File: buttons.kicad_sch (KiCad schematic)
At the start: 11 parts, among them SW1 power, SW2 up, SW3 down, SW4 left, SW5 rigth

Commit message: Fix KiCad 10 footprint library: register kiC library, fix schematic references
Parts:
- SW1, SW3, SW4, SW5: footprint Button_Switch_SMD:SW_Push_1P1T_NO_6x6mm_H9.5mm -> kiC:SW_Push_1P1T_NO_6x6mm_H9.5mm
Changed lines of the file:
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@@
 			)
 		)
-		(property "Footprint" "Button_Switch_SMD:SW_Push_1P1T_NO_6x6mm_H9.5mm"
+		(property "Footprint" "kiC:SW_Push_1P1T_NO_6x6mm_H9.5mm"
 			(at 212.09 110.49 0)
 			(hide yes)
@@
 			)
 		)
-		(property "Footprint" "Button_Switch_SMD:SW_Push_1P1T_NO_6x6mm_H9.5mm"
+		(property "Footprint" "kiC:SW_Push_1P1T_NO_6x6mm_H9.5mm"
 			(at 137.16 77.47 0)
 			(hide yes)
@@
 			)
 		)
-		(property "Footprint" "Button_Switch_SMD:SW_Push_1P1T_NO_6x6mm_H9.5mm"
+		(property "Footprint" "kiC:SW_Push_1P1T_NO_6x6mm_H9.5mm"
 			(at 144.78 123.19 0)
 			(hide yes)
@@
 			)
 		)
-		(property "Footprint" "Button_Switch_SMD:SW_Push_1P1T_NO_6x6mm_H9.5mm"
+		(property "Footprint" "kiC:SW_Push_1P1T_NO_6x6mm_H9.5mm"
 			(at 212.09 97.79 0)
 			(hide yes)

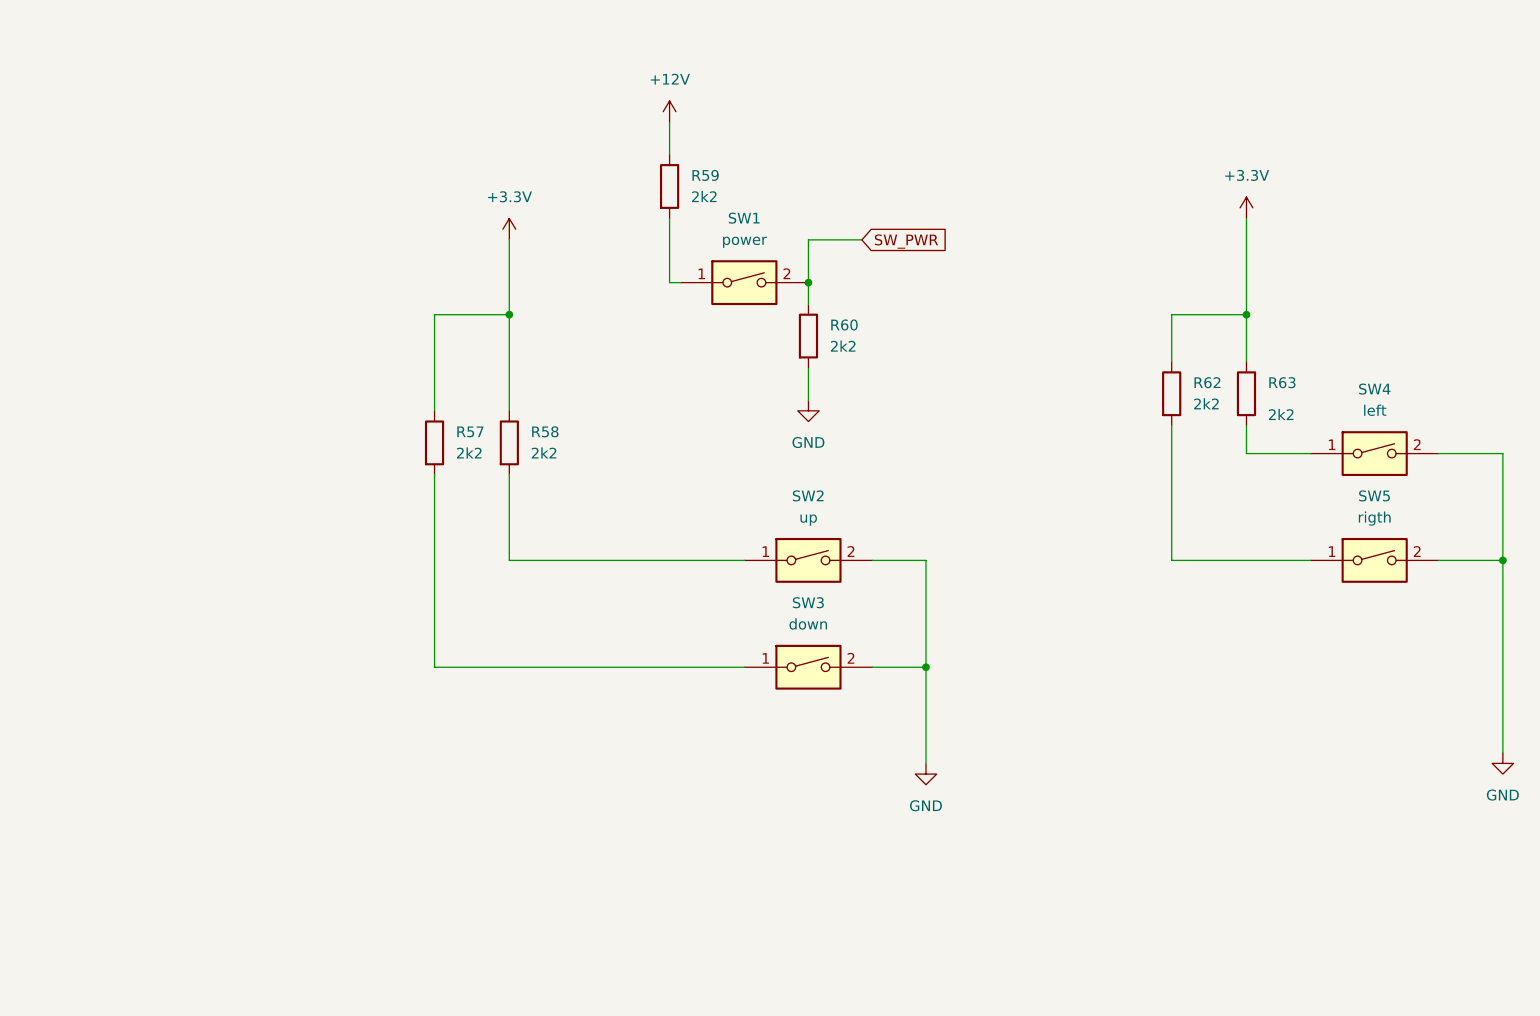
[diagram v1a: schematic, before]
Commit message: feat: 25 hierarchical labels for 5 Pololus + fix J4/J15/J17/TP17 footprints + USB pin6→SH
- pololu.kicad_sch: 5→25 hierarchical labels (reset_N, sleep_N, enable_N, step_N, dir_N) with wires to each Pololu A4988
- pololu.kicad_sch: J17 footprint kiC:PinHeader → Library:PinHeader_1x06_P2.54mm_Vertical
- cnc_pic32.kicad_sch: expanded Pololu sheet box with 25 named sheet pins
- buttons.kicad_sch: all SW switches → Button_Switch_SMD:SW_SPST_CK_RS282G05A3
- tp_ft232.kicad_sch: kiC:pad_0508 + kiC:Pin_D1.5mmx1mm → Library:connector_pin1
- usb_conector_Ft232.kicad_sch: J4/J15 kiC:Pin_D1.5mmx1mm → Library:connector_pin1, J5 pin 6→SH
- Usb_pic32.kicad_sch: TP17 kiC:Pin_D1.5mmx1mm → Library:connector_pin1, J18 pin 6→SH
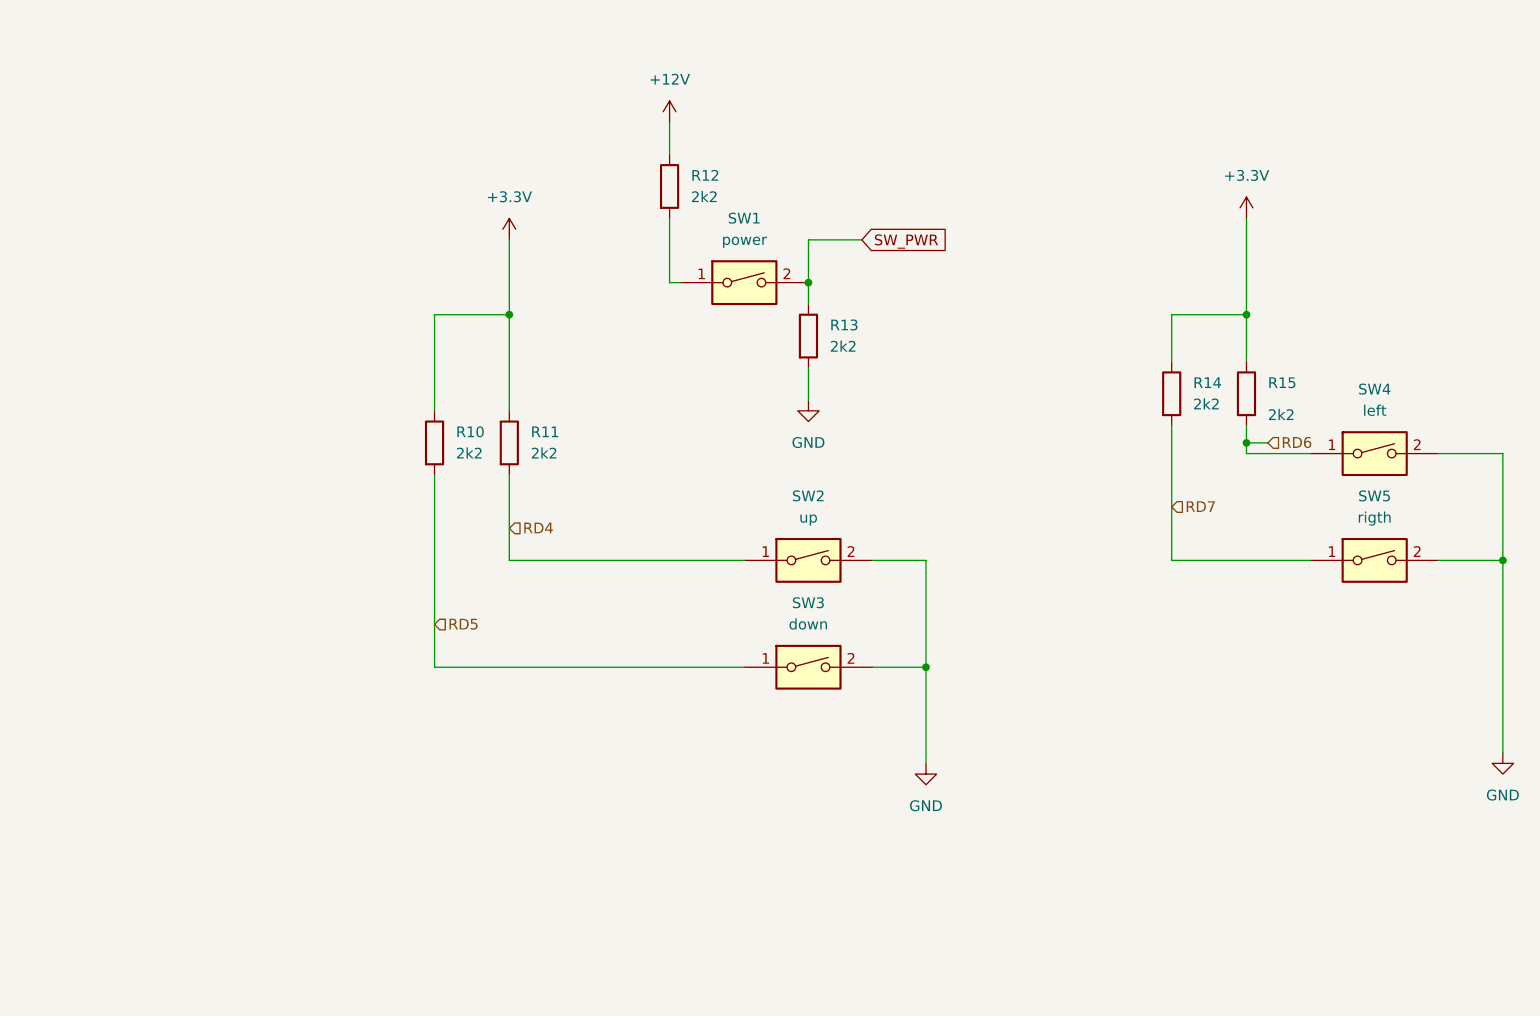
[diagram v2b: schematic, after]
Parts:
- SW1, SW3, SW4, SW5: footprint kiC:SW_Push_1P1T_NO_6x6mm_H9.5mm -> Button_Switch_SMD:SW_SPST_CK_RS282G05A3
- renumbered R57 to R10, R58 to R11, R59 to R12, R60 to R13, R62 to R14, R63 to R15
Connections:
- net RD7: now reaches R14.2, SW5.1
- net RD6: now reaches R15.2, SW4.1
- net RD5: now reaches R10.2, SW3.1
- net RD4: now reaches R11.2, SW2.1
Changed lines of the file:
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@@
 	(paper "A4")
+	(junction
+		(at 196.85 96.52)
+		(diameter 0)
+		(color 0 0 0 0)
+	)
 	(junction
 		(at 109.22 81.28)
@@
 	(wire
 		(pts
-			(xy 196.85 97.79) (xy 196.85 94.488)
+			(xy 196.85 96.52) (xy 199.39 96.52)
+		)
+		(stroke
+			(width 0)
+			(type default)
+		)
+	)
+	(wire
+		(pts
+			(xy 196.85 97.79) (xy 196.85 96.52)
 		)
 		(stroke
@@
 		(pts
 			(xy 152.4 110.49) (xy 158.75 110.49)
+		)
+		(stroke
+			(width 0)
+			(type default)
+		)
+	)
+	(wire
+		(pts
+			(xy 196.85 96.52) (xy 196.85 94.488)
 		)
 		(stroke
@@
 				(justify left)
 			)
+		)
+	)
+	(hierarchical_label "RD4"
+		(shape input)
+		(at 109.22 106.68 0)
+		(effects
+			(font
+				(size 1.27 1.27)
+			)
+			(justify left)
+		)
+	)
+	(hierarchical_label "RD5"
+		(shape input)
+		(at 100.33 118.11 0)
+		(effects
+			(font
+				(size 1.27 1.27)
+			)
+			(justify left)
+		)
+	)
+	(hierarchical_label "RD7"
+		(shape input)
+		(at 187.96 104.14 0)
+		(effects
+			(font
+				(size 1.27 1.27)
+			)
+			(justify left)
+		)
+	)
+	(hierarchical_label "RD6"
+		(shape input)
+		(at 199.39 96.52 0)
+		(effects
+			(font
+				(size 1.27 1.27)
+			)
+			(justify left)
 		)
 	)
@@
 			)
 		)
-		(property "Footprint" "kiC:SW_Push_1P1T_NO_6x6mm_H9.5mm"
+		(property "Footprint" "Button_Switch_SMD:SW_SPST_CK_RS282G05A3"
 			(at 212.09 110.49 0)
 			(hide yes)
@@
 			)
 		)
-		(property "Footprint" "kiC:SW_Push_1P1T_NO_6x6mm_H9.5mm"
+		(property "Footprint" "Button_Switch_SMD:SW_SPST_CK_RS282G05A3"
 			(at 137.16 77.47 0)
 			(hide yes)
@@
 		(dnp no)
 		(fields_autoplaced yes)
-		(property "Reference" "R62"
+		(property "Reference" "R14"
 			(at 190.5 89.408 0)
 			(show_name no)
@@
 			(project "cnc_pic32"
 				(path "/13dbfc1f-be47-44ca-9042-3d6a9a657d7d/64cf98d4-7353-423c-baad-4e05534717be/fed6e348-19f5-499e-8dbd-e696ef87e744"
-					(reference "R62")
+					(reference "R14")
 					(unit 1)
 				)
@@
 		(in_pos_files yes)
 		(dnp no)
-		(property "Reference" "R63"
+		(property "Reference" "R15"
 			(at 199.39 89.408 0)
 			(show_name no)
@@
 			(project "cnc_pic32"
 				(path "/13dbfc1f-be47-44ca-9042-3d6a9a657d7d/64cf98d4-7353-423c-baad-4e05534717be/fed6e348-19f5-499e-8dbd-e696ef87e744"
-					(reference "R63")
+					(reference "R15")
 					(unit 1)
 				)
@@
 		(dnp no)
 		(fields_autoplaced yes)
-		(property "Reference" "#PWR092"
+		(property "Reference" "#PWR017"
 			(at 227.33 139.7 0)
 			(hide yes)
@@
 			(project "cnc_pic32"
 				(path "/13dbfc1f-be47-44ca-9042-3d6a9a657d7d/64cf98d4-7353-423c-baad-4e05534717be/fed6e348-19f5-499e-8dbd-e696ef87e744"
-					(reference "#PWR092")
+					(reference "#PWR017")
 					(unit 1)
 				)
@@
 		(dnp no)
 		(fields_autoplaced yes)
-		(property "Reference" "R60"
+		(property "Reference" "R13"
 			(at 147.32 82.5499 0)
 			(show_name no)
@@
 			(project "cnc_pic32"
 				(path "/13dbfc1f-be47-44ca-9042-3d6a9a657d7d/64cf98d4-7353-423c-baad-4e05534717be/fed6e348-19f5-499e-8dbd-e696ef87e744"
-					(reference "R60")
+					(reference "R13")
 					(unit 1)
 				)
@@
 		(dnp no)
 		(fields_autoplaced yes)
-		(property "Reference" "R57"
+		(property "Reference" "R10"
 			(at 102.87 95.2499 0)
 			(show_name no)
@@
 			(project "cnc_pic32"
 				(path "/13dbfc1f-be47-44ca-9042-3d6a9a657d7d/64cf98d4-7353-423c-baad-4e05534717be/fed6e348-19f5-499e-8dbd-e696ef87e744"
-					(reference "R57")
+					(reference "R10")
 					(unit 1)
 				)
@@
 			)
 		)
-		(property "Footprint" "kiC:SW_Push_1P1T_NO_6x6mm_H9.5mm"
+		(property "Footprint" "Button_Switch_SMD:SW_SPST_CK_RS282G05A3"
 			(at 144.78 123.19 0)
 			(hide yes)
@@
 		(dnp no)
 		(fields_autoplaced yes)
-		(property "Reference" "#PWR089"
+		(property "Reference" "#PWR014"
 			(at 144.78 97.79 0)
 			(hide yes)
@@
 			(project "cnc_pic32"
 				(path "/13dbfc1f-be47-44ca-9042-3d6a9a657d7d/64cf98d4-7353-423c-baad-4e05534717be/fed6e348-19f5-499e-8dbd-e696ef87e744"
-					(reference "#PWR089")
+					(reference "#PWR014")
 					(unit 1)
 				)
@@
 			)
 		)
-		(property "Footprint" "kiC:SW_Push_1P1T_NO_6x6mm_H9.5mm"
+		(property "Footprint" "Button_Switch_SMD:SW_SPST_CK_RS282G05A3"
 			(at 212.09 97.79 0)
 			(hide yes)
@@
 		(dnp no)
 		(fields_autoplaced yes)
-		(property "Reference" "#PWR087"
+		(property "Reference" "#PWR012"
 			(at 109.22 76.2 0)
 			(hide yes)
@@
 			(project "cnc_pic32"
 				(path "/13dbfc1f-be47-44ca-9042-3d6a9a657d7d/64cf98d4-7353-423c-baad-4e05534717be/fed6e348-19f5-499e-8dbd-e696ef87e744"
-					(reference "#PWR087")
+					(reference "#PWR012")
 					(unit 1)
 				)
@@
 		(dnp no)
 		(fields_autoplaced yes)
-		(property "Reference" "#PWR090"
+		(property "Reference" "#PWR015"
 			(at 158.75 140.97 0)
 			(hide yes)
@@
 			(project "cnc_pic32"
 				(path "/13dbfc1f-be47-44ca-9042-3d6a9a657d7d/64cf98d4-7353-423c-baad-4e05534717be/fed6e348-19f5-499e-8dbd-e696ef87e744"
-					(reference "#PWR090")
+					(reference "#PWR015")
 					(unit 1)
 				)
@@
 		(dnp no)
 		(fields_autoplaced yes)
-		(property "Reference" "R58"
+		(property "Reference" "R11"
 			(at 111.76 95.2499 0)
 			(show_name no)
@@
 			(project "cnc_pic32"
 				(path "/13dbfc1f-be47-44ca-9042-3d6a9a657d7d/64cf98d4-7353-423c-baad-4e05534717be/fed6e348-19f5-499e-8dbd-e696ef87e744"
-					(reference "R58")
+					(reference "R11")
 					(unit 1)
 				)
@@
 		(dnp no)
 		(fields_autoplaced yes)
-		(property "Reference" "#PWR091"
+		(property "Reference" "#PWR016"
 			(at 196.85 73.66 0)
 			(hide yes)
@@
 			(project "cnc_pic32"
 				(path "/13dbfc1f-be47-44ca-9042-3d6a9a657d7d/64cf98d4-7353-423c-baad-4e05534717be/fed6e348-19f5-499e-8dbd-e696ef87e744"
-					(reference "#PWR091")
+					(reference "#PWR016")
 					(unit 1)
 				)
@@
 		(dnp no)
 		(fields_autoplaced yes)
-		(property "Reference" "#PWR088"
+		(property "Reference" "#PWR013"
 			(at 128.27 62.23 0)
 			(hide yes)
@@
 			(project "cnc_pic32"
 				(path "/13dbfc1f-be47-44ca-9042-3d6a9a657d7d/64cf98d4-7353-423c-baad-4e05534717be/fed6e348-19f5-499e-8dbd-e696ef87e744"
-					(reference "#PWR088")
+					(reference "#PWR013")
 					(unit 1)
 				)
@@
 		(dnp no)
 		(fields_autoplaced yes)
-		(property "Reference" "R59"
+		(property "Reference" "R12"
 			(at 130.81 64.77 0)
 			(show_name no)
@@
 			(project "cnc_pic32"
 				(path "/13dbfc1f-be47-44ca-9042-3d6a9a657d7d/64cf98d4-7353-423c-baad-4e05534717be/fed6e348-19f5-499e-8dbd-e696ef87e744"
-					(reference "R59")
+					(reference "R12")
 					(unit 1)
 				)

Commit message: fix: unify +3.3V to +3V3 across all schematics and PCB
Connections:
- net +3.3V: no longer names the net of R14.1, R15.1
- net +3.3V: no longer R10.1, R11.1
- new net: R10.1, R11.1
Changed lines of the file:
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@@
 	)
 	(symbol
-		(lib_id "power:+3.3V")
+		(lib_id "power:+3V3")
 		(at 109.22 72.39 0)
 		(unit 1)
@@
 			)
 		)
-		(property "Value" "+3.3V"
+		(property "Value" "+3V3"
 			(at 109.22 67.31 0)
 			(show_name no)
@@
 	)
 	(symbol
-		(lib_id "power:+3.3V")
+		(lib_id "power:+3V3")
 		(at 196.85 69.85 0)
 		(unit 1)
@@
 			)
 		)
-		(property "Value" "+3.3V"
+		(property "Value" "+3V3"
 			(at 196.85 64.77 0)
 			(show_name no)

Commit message: feat: integrate zigbee sheet + R 0603→0805 footprint update
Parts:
- R14, R15: footprint Resistor_SMD:R_0603_1608Metric -> Resistor_SMD:R_0805_2012Metric
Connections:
- net +3.3V: now reaches R14.1, R15.1
- net +3.3V: now also R10.1, R11.1
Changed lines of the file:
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@@
 			)
 		)
-		(property "Footprint" "Resistor_SMD:R_0603_1608Metric"
+		(property "Footprint" "Resistor_SMD:R_0805_2012Metric"
 			(at 186.182 90.678 90)
 			(hide yes)
@@
 			)
 		)
-		(property "Footprint" "Resistor_SMD:R_0603_1608Metric"
+		(property "Footprint" "Resistor_SMD:R_0805_2012Metric"
 			(at 195.072 90.678 90)
 			(hide yes)
@@
 	)
 	(symbol
+		(lib_id "power:+3.3V")
+		(at 196.85 69.85 0)
+		(unit 1)
+		(body_style 1)
+		(exclude_from_sim no)
+		(in_bom yes)
+		(on_board yes)
+		(in_pos_files yes)
+		(dnp no)
+		(fields_autoplaced yes)
+		(property "Reference" "#PWR018"
+			(at 196.85 73.66 0)
+			(hide yes)
+			(show_name no)
+			(do_not_autoplace no)
+			(effects
+				(font
+					(size 1.27 1.27)
+				)
+			)
+		)
+		(property "Value" "+3.3V"
+			(at 196.85 64.77 0)
+			(show_name no)
+			(do_not_autoplace no)
+			(effects
+				(font
+					(size 1.27 1.27)
+				)
+			)
+		)
+		(property "Footprint" ""
+			(at 196.85 69.85 0)
+			(hide yes)
+			(show_name no)
+			(do_not_autoplace no)
+			(effects
+				(font
+					(size 1.27 1.27)
+				)
+			)
+		)
+		(property "Datasheet" ""
+			(at 196.85 69.85 0)
+			(hide yes)
+			(show_name no)
+			(do_not_autoplace no)
+			(effects
+				(font
+					(size 1.27 1.27)
+				)
+			)
+		)
+		(property "Description" ""
+			(at 196.85 69.85 0)
+			(show_name no)
+			(do_not_autoplace no)
+			(effects
+				(font
+					(size 1.27 1.27)
+				)
+			)
+		)
+		(pin "1"
+		)
+		(instances
+			(project "cnc_pic32"
+				(path "/13dbfc1f-be47-44ca-9042-3d6a9a657d7d/64cf98d4-7353-423c-baad-4e05534717be/fed6e348-19f5-499e-8dbd-e696ef87e744"
+					(reference "#PWR018")
+					(unit 1)
+				)
+			)
+		)
+	)
+	(symbol
 		(lib_id "Switch:SW_DIP_x01")
 		(at 144.78 123.19 0)
@@
 	)
 	(symbol
-		(lib_id "power:+3V3")
+		(lib_id "power:+3.3V")
 		(at 109.22 72.39 0)
 		(unit 1)
@@
 			)
 		)
-		(property "Value" "+3V3"
+		(property "Value" "+3.3V"
 			(at 109.22 67.31 0)
 			(show_name no)
@@
 					(unit 1)
 				)
-			)
-		)
-	)
-	(symbol
-		(lib_id "power:+3V3")
-		(at 196.85 69.85 0)
-		(unit 1)
-		(body_style 1)
-		(exclude_from_sim no)
-		(in_bom yes)
-		(on_board yes)
-		(in_pos_files yes)
-		(dnp no)
-		(fields_autoplaced yes)
-		(property "Reference" "#PWR018"
-			(at 196.85 73.66 0)
-			(hide yes)
-			(show_name no)
-			(do_not_autoplace no)
-			(effects
-				(font
-					(size 1.27 1.27)
-				)
-			)
-		)
-		(property "Value" "+3V3"
-			(at 196.85 64.77 0)
-			(show_name no)
-			(do_not_autoplace no)
-			(effects
-				(font
-					(size 1.27 1.27)
-				)
-			)
-		)
-		(property "Footprint" ""
-			(at 196.85 69.85 0)
-			(hide yes)
-			(show_name no)
-			(do_not_autoplace no)
-			(effects
-				(font
-					(size 1.27 1.27)
-				)
-			)
-		)
-		(property "Datasheet" ""
-			(at 196.85 69.85 0)
-			(hide yes)
-			(show_name no)
-			(do_not_autoplace no)
-			(effects
-				(font
-					(size 1.27 1.27)
-				)
-			)
-		)
-		(property "Description" ""
-			(at 196.85 69.85 0)
-			(show_name no)
-			(do_not_autoplace no)
-			(effects
-				(font
-					(size 1.27 1.27)
-				)
-			)
-		)
-		(pin "1"
-		)
-		(instances
-			(project "cnc_pic32"
-				(path "/13dbfc1f-be47-44ca-9042-3d6a9a657d7d/64cf98d4-7353-423c-baad-4e05534717be/fed6e348-19f5-499e-8dbd-e696ef87e744"
-					(reference "#PWR018")
-					(unit 1)
-				)
